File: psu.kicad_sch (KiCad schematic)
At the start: 6 parts, among them U1 AMS1117-3.3, U2 AMS1117-5.0

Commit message: WIP filters
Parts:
- C1, C5, C7, C8: symbol Device:C -> Device:C_Small
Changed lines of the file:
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@@
+    (stroke (width 0) (type default))
+  )
+  (wire (pts (xy 139.7 102.87) (xy 139.7 104.14))
     (stroke (width 0) (type default))
   )
@@
     (stroke (width 0) (type default))
   )
-  (wire (pts (xy 139.7 93.98) (xy 139.7 96.52))
-    (stroke (width 0) (type default))
-  )
-  (wire (pts (xy 152.4 93.98) (xy 152.4 96.52))
+  (wire (pts (xy 139.7 93.98) (xy 139.7 97.79))
+    (stroke (width 0) (type default))
+  )
+  (wire (pts (xy 152.4 102.87) (xy 152.4 104.14))
+    (stroke (width 0) (type default))
+  )
+  (wire (pts (xy 114.3 102.87) (xy 114.3 104.14))
+    (stroke (width 0) (type default))
+  )
+  (wire (pts (xy 152.4 93.98) (xy 152.4 97.79))
     (stroke (width 0) (type default))
   )
@@
     (stroke (width 0) (type default))
   )
-  (wire (pts (xy 177.8 93.98) (xy 177.8 96.52))
+  (wire (pts (xy 177.8 93.98) (xy 177.8 97.79))
     (stroke (width 0) (type default))
   )
@@
     (stroke (width 0) (type default))
   )
-  (wire (pts (xy 114.3 93.98) (xy 114.3 96.52))
+  (wire (pts (xy 114.3 93.98) (xy 114.3 97.79))
     (stroke (width 0) (type default))
   )
@@
     (stroke (width 0) (type default))
   )
+  (wire (pts (xy 177.8 102.87) (xy 177.8 104.14))
+    (stroke (width 0) (type default))
+  )
   (wire (pts (xy 165.1 101.6) (xy 165.1 104.14))
     (stroke (width 0) (type default))
   )
-  (symbol (lib_id "Device:C") (at 114.3 100.33 0) (unit 1)
+  (symbol (lib_id "Device:C_Small") (at 114.3 100.33 0) (unit 1)
     (in_bom yes) (on_board yes) (dnp no) (fields_autoplaced)
     (property "Reference" "C1" (at 117.221 99.1179 0)
@@
       (effects (font (size 1.27 1.27)) (justify left))
     )
-    (property "Footprint" "Capacitor_SMD:C_0805_2012Metric" (at 115.2652 104.14 0)
+    (property "Footprint" "Capacitor_SMD:C_0805_2012Metric" (at 114.3 100.33 0)
       (effects (font (size 1.27 1.27)) hide)
     )
@@
     )
   )
-  (symbol (lib_id "Device:C") (at 152.4 100.33 0) (unit 1)
+  (symbol (lib_id "Device:C_Small") (at 152.4 100.33 0) (unit 1)
     (in_bom yes) (on_board yes) (dnp no) (fields_autoplaced)
     (property "Reference" "C7" (at 155.321 99.1179 0)
@@
       (effects (font (size 1.27 1.27)) (justify left))
     )
-    (property "Footprint" "Capacitor_SMD:C_0805_2012Metric" (at 153.3652 104.14 0)
+    (property "Footprint" "Capacitor_SMD:C_0805_2012Metric" (at 152.4 100.33 0)
       (effects (font (size 1.27 1.27)) hide)
     )
@@
     )
   )
-  (symbol (lib_id "Device:C") (at 177.8 100.33 0) (unit 1)
+  (symbol (lib_id "Device:C_Small") (at 177.8 100.33 0) (unit 1)
     (in_bom yes) (on_board yes) (dnp no) (fields_autoplaced)
     (property "Reference" "C8" (at 180.721 99.1179 0)
@@
       (effects (font (size 1.27 1.27)) (justify left))
     )
-    (property "Footprint" "Capacitor_SMD:C_0603_1608Metric" (at 178.7652 104.14 0)
+    (property "Footprint" "Capacitor_SMD:C_0603_1608Metric" (at 177.8 100.33 0)
       (effects (font (size 1.27 1.27)) hide)
     )
@@
     )
   )
-  (symbol (lib_id "Device:C") (at 139.7 100.33 0) (unit 1)
+  (symbol (lib_id "Device:C_Small") (at 139.7 100.33 0) (unit 1)
     (in_bom yes) (on_board yes) (dnp no) (fields_autoplaced)
     (property "Reference" "C5" (at 142.621 99.1179 0)
@@
       (effects (font (size 1.27 1.27)) (justify left))
     )
-    (property "Footprint" "Capacitor_SMD:C_0603_1608Metric" (at 140.6652 104.14 0)
-      (effects (font (size 1.27 1.27)) hide)
-    )
+    (property "Footprint" "Capacitor_SMD:C_0603_1608Metric" (at 139.7 100.33 0)
+      (effects (font (size 1.27 1.27)) hide)
+    )

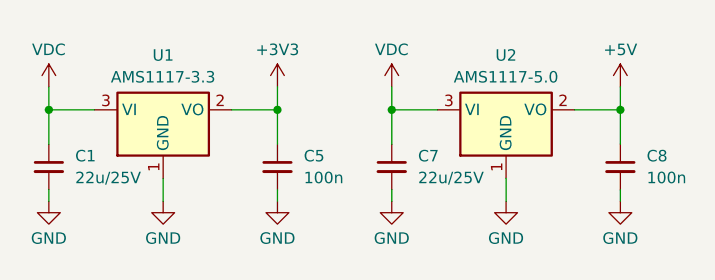
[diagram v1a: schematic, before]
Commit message: First Edits
Added J1 connector, finished filters and swapped µC to STM32G473
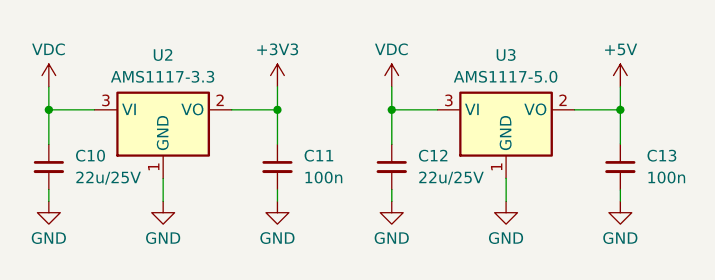
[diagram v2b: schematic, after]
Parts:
- C11: renamed from C5; footprint Capacitor_SMD:C_0603_1608Metric -> Capacitor_SMD:C_0201_0603Metric
- C13: renamed from C8; footprint Capacitor_SMD:C_0603_1608Metric -> Capacitor_SMD:C_0201_0603Metric
- renumbered C1 to C10, C7 to C12, U1 to U2, U2 to U3

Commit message: PCB routed, gerbers and ibom included
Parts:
- removed C12: 22u/25V, Capacitor_SMD:C_0805_2012Metric, symbol Device:C_Small
- removed U2: AMS1117-3.3, Package_TO_SOT_SMD:SOT-223-3_TabPin2, symbol Regulator_Linear:AMS1117-3.3
- removed U3: AMS1117-5.0, Package_TO_SOT_SMD:SOT-223-3_TabPin2, symbol Regulator_Linear:AMS1117-5.0
- added U2: XC6220B331MR, Package_TO_SOT_SMD:SOT-23-5, symbol Regulator_Linear:XC6220B331MR
- C11, C13: footprint Capacitor_SMD:C_0201_0603Metric -> Capacitor_SMD:C_0402_1005Metric
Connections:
- net VDC is gone; now on net +5V: C10.1
- net +3V3: now also U2.5 (VOUT)
- net +5V: now also U2.1 (VIN), U2.3 (CE)
- net GND: now also U2.2 (GND)
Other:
- moved on the sheet: C10, C11, C13

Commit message: LCSC part numbers included into schematics
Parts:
- C10: LCSC (none) -> C45783
- C11, C13: LCSC (none) -> C56392
- U2: LCSC (none) -> C3040644
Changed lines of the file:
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@@
 			)
 		)
-		(property "LCSC Part#" ""
+		(property "Height" ""
+			(at 133.35 99.06 0)
+			(effects
+				(font
+					(size 1.27 1.27)
+				)
+				(hide yes)
+			)
+		)
+		(property "Manufacturer_Name" ""
+			(at 133.35 99.06 0)
+			(effects
+				(font
+					(size 1.27 1.27)
+				)
+				(hide yes)
+			)
+		)
+		(property "Manufacturer_Part_Number" ""
+			(at 133.35 99.06 0)
+			(effects
+				(font
+					(size 1.27 1.27)
+				)
+				(hide yes)
+			)
+		)
+		(property "Mouser Part Number" ""
+			(at 133.35 99.06 0)
+			(effects
+				(font
+					(size 1.27 1.27)
+				)
+				(hide yes)
+			)
+		)
+		(property "Mouser Price/Stock" ""
+			(at 133.35 99.06 0)
+			(effects
+				(font
+					(size 1.27 1.27)
+				)
+				(hide yes)
+			)
+		)
+		(property "LCSC" "C45783"
+			(at 133.35 99.06 0)
+			(effects
+				(font
+					(size 1.27 1.27)
+				)
+				(hide yes)
+			)
+		)
+		(property "JLC" ""
 			(at 133.35 99.06 0)
 			(effects
@@
 			)
 		)
+		(property "Height" ""
+			(at 154.94 95.25 0)
+			(effects
+				(font
+					(size 1.27 1.27)
+				)
+				(hide yes)
+			)
+		)
+		(property "Manufacturer_Name" ""
+			(at 154.94 95.25 0)
+			(effects
+				(font
+					(size 1.27 1.27)
+				)
+				(hide yes)
+			)
+		)
+		(property "Manufacturer_Part_Number" ""
+			(at 154.94 95.25 0)
+			(effects
+				(font
+					(size 1.27 1.27)
+				)
+				(hide yes)
+			)
+		)
+		(property "Mouser Part Number" ""
+			(at 154.94 95.25 0)
+			(effects
+				(font
+					(size 1.27 1.27)
+				)
+				(hide yes)
+			)
+		)
+		(property "Mouser Price/Stock" ""
+			(at 154.94 95.25 0)
+			(effects
+				(font
+					(size 1.27 1.27)
+				)
+				(hide yes)
+			)
+		)
+		(property "LCSC" "C3040644"
+			(at 154.94 95.25 0)
+			(effects
+				(font
+					(size 1.27 1.27)
+				)
+				(hide yes)
+			)
+		)
+		(property "JLC" ""
+			(at 154.94 95.25 0)
+			(effects
+				(font
+					(size 1.27 1.27)
+				)
+				(hide yes)
+			)
+		)
 		(pin "4"
 		)
@@
 			)
 		)
-		(property "LCSC Part#" ""
+		(property "Height" ""
+			(at 119.38 99.06 0)
+			(effects
+				(font
+					(size 1.27 1.27)
+				)
+				(hide yes)
+			)
+		)
+		(property "Manufacturer_Name" ""
+			(at 119.38 99.06 0)
+			(effects
+				(font
+					(size 1.27 1.27)
+				)
+				(hide yes)
+			)
+		)
+		(property "Manufacturer_Part_Number" ""
+			(at 119.38 99.06 0)
+			(effects
+				(font
+					(size 1.27 1.27)
+				)
+				(hide yes)
+			)
+		)
+		(property "Mouser Part Number" ""
+			(at 119.38 99.06 0)
+			(effects
+				(font
+					(size 1.27 1.27)
+				)
+				(hide yes)
+			)
+		)
+		(property "Mouser Price/Stock" ""
+			(at 119.38 99.06 0)
+			(effects
+				(font
+					(size 1.27 1.27)
+				)
+				(hide yes)
+			)
+		)
+		(property "LCSC" "C56392"
+			(at 119.38 99.06 0)
+			(effects
+				(font
+					(size 1.27 1.27)
+				)
+				(hide yes)
+			)
+		)
+		(property "JLC" ""
 			(at 119.38 99.06 0)
 			(effects
@@
 			)
 		)
-		(property "LCSC Part#" ""
-			(at 172.72 99.06 0)
-			(effects
+		(property "Height" ""
+			(at 172.72 99.06 0)
+			(effects
+				(font
+					(size 1.27 1.27)
+				)
+				(hide yes)
+			)
+		)
+		(property "Manufacturer_Name" ""
+			(at 172.72 99.06 0)
+			(effects
+				(font
+					(size 1.27 1.27)
+				)
+				(hide yes)
+			)
+		)
+		(property "Manufacturer_Part_Number" ""
+			(at 172.72 99.06 0)
+			(effects
+				(font
+					(size 1.27 1.27)
+				)
+				(hide yes)
+			)
+		)
+		(property "Mouser Part Number" ""
+			(at 172.72 99.06 0)
+			(effects
+				(font
+					(size 1.27 1.27)
+				)
+				(hide yes)
+			)
+		)
+		(property "Mouser Price/Stock" ""
+			(at 172.72 99.06 0)
+			(effects
+				(font
+					(size 1.27 1.27)
+				)
+				(hide yes)
+			)
+		)
+		(property "LCSC" "C56392"
+			(at 172.72 99.06 0)
+			(effects
+				(font
+					(size 1.27 1.27)
+				)
+				(hide yes)
+			)
+		)
+		(property "JLC" ""
+			(at 172.72 99.06 0)
+			(effects

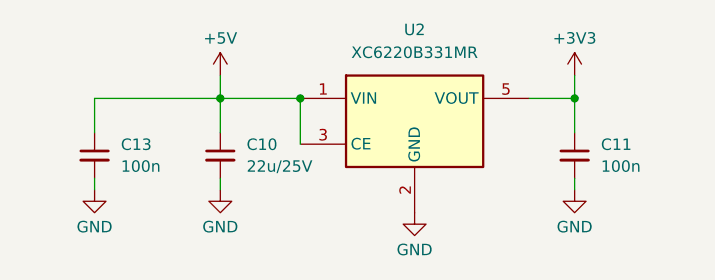
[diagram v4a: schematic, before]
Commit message: PA2 Bias add, USB conn add.
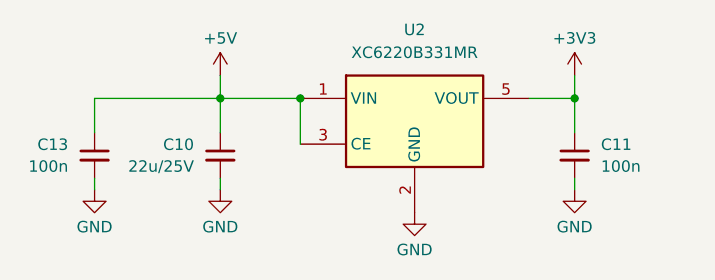
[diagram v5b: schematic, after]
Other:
- title: Micro17 - OpenRTX on a Module -> Micro17 - OpenRTX on a Module for Icom Radios
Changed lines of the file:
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@@
 	(paper "A4")
 	(title_block
-		(title "Micro17 - OpenRTX on a Module")
-		(date "05.12.2023")
+		(title "Micro17 - OpenRTX on a Module for Icom Radios")
+		(date "04.03.2024")
 		(rev "A")
 		(company "Wojciech Kaczmarski SP5WWP et al.")
 		(comment 1 "M17 Project, OpenRTX")
+		(comment 2 "Mano ON6RF")
+		(comment 3 "Mutlu TA1MD")
 	)
 	(junction
@@
 		(lib_id "Device:C_Small")
 		(at 133.35 99.06 0)
+		(mirror y)
 		(unit 1)
 		(exclude_from_sim no)
@@
 		(on_board yes)
 		(dnp no)
-		(fields_autoplaced yes)
 		(property "Reference" "C10"
-			(at 136.271 97.8479 0)
+			(at 130.429 97.8479 0)
 			(effects
 				(font
@@
 		)
 		(property "Value" "22u/25V"
-			(at 136.271 100.2721 0)
+			(at 130.429 100.2721 0)
 			(effects
 				(font
@@
 		(lib_id "Device:C_Small")
 		(at 119.38 99.06 0)
+		(mirror y)
 		(unit 1)
 		(exclude_from_sim no)
@@
 		(on_board yes)
 		(dnp no)
-		(fields_autoplaced yes)
 		(property "Reference" "C13"
-			(at 122.301 97.8479 0)
+			(at 116.459 97.8479 0)
 			(effects
 				(font
@@
 		)
 		(property "Value" "100n"
-			(at 122.301 100.2721 0)
-			(effects
-				(font
+			(at 116.459 100.2721 0)
+			(effects
+				(font

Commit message: cosmetic changes to the schematic layout
- R25 - DNP
- PDF render update
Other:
- company: Wojciech Kaczmarski SP5WWP et al. -> Wojciech SP5WWP, Mano ON6RF, Mutlu TA1MD et al.
- title: Micro17 - OpenRTX on a Module for Icom Radios -> Micro17 - OpenRTX on a Module for ICOM radios
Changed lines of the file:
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@@
 	(paper "A4")
 	(title_block
-		(title "Micro17 - OpenRTX on a Module for Icom Radios")
-		(date "04.03.2024")
+		(title "Micro17 - OpenRTX on a Module for ICOM radios")
+		(date "06.03.2024")
 		(rev "A")
-		(company "Wojciech Kaczmarski SP5WWP et al.")
+		(company "Wojciech SP5WWP, Mano ON6RF, Mutlu TA1MD et al.")
 		(comment 1 "M17 Project, OpenRTX")
 		(comment 2 "Mano ON6RF")

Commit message: Bias voltage changed, usart rx tp add
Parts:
- C10: MPN (none) -> C45783
- C11, C13: MPN (none) -> C56392
- U2: MPN (none) -> C3040644
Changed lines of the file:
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@@
 			)
 		)
-		(property "MPN" ""
+		(property "MPN" "C45783"
 			(at 133.35 99.06 0)
 			(effects
@@
 		)
 		(property "JLC" ""
+			(at 133.35 99.06 0)
+			(effects
+				(font
+					(size 1.27 1.27)
+				)
+				(hide yes)
+			)
+		)
+		(property "PN" ""
 			(at 133.35 99.06 0)
 			(effects
@@
 			)
 		)
+		(property "PN" ""
+			(at 154.94 95.25 0)
+			(effects
+				(font
+					(size 1.27 1.27)
+				)
+				(hide yes)
+			)
+		)
+		(property "MPN" "C3040644"
+			(at 154.94 95.25 0)
+			(effects
+				(font
+					(size 1.27 1.27)
+				)
+				(hide yes)
+			)
+		)
 		(pin "4"
 		)
@@
 			)
 		)
-		(property "MPN" ""
+		(property "MPN" "C56392"
 			(at 119.38 99.06 0)
 			(effects
@@
 		)
 		(property "JLC" ""
+			(at 119.38 99.06 0)
+			(effects
+				(font
+					(size 1.27 1.27)
+				)
+				(hide yes)
+			)
+		)
+		(property "PN" ""
 			(at 119.38 99.06 0)
 			(effects
@@
 			)
 		)
-		(property "MPN" ""
+		(property "MPN" "C56392"
 			(at 172.72 99.06 0)
 			(effects
@@
 			(at 172.72 99.06 0)
 			(effects
+				(font
+					(size 1.27 1.27)
+				)
+				(hide yes)
+			)
+		)
+		(property "PN" ""
+			(at 172.72 99.06 0)
+			(effects
